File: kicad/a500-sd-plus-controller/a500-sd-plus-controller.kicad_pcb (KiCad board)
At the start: 2 copper layers, 65 x 54 mm, 57 parts, among them J1 Micro_SD_Card_Det2, J2 AUX_SPI, J3 Micro_SD_Card_Det2, J4 JTAG, J5 Conn_01x02, K1 DIP_socket_40pins, U1 RT9013-18, U10 RT9013-33, U2 5M160ZE64, U3 SN74LVC8T245, U4 CSG8520_CIA, U5 SRV05-4, U6 SN74LVC8T245, U7 RT9013-33, U8 RT9013-33, Y1 16MHz

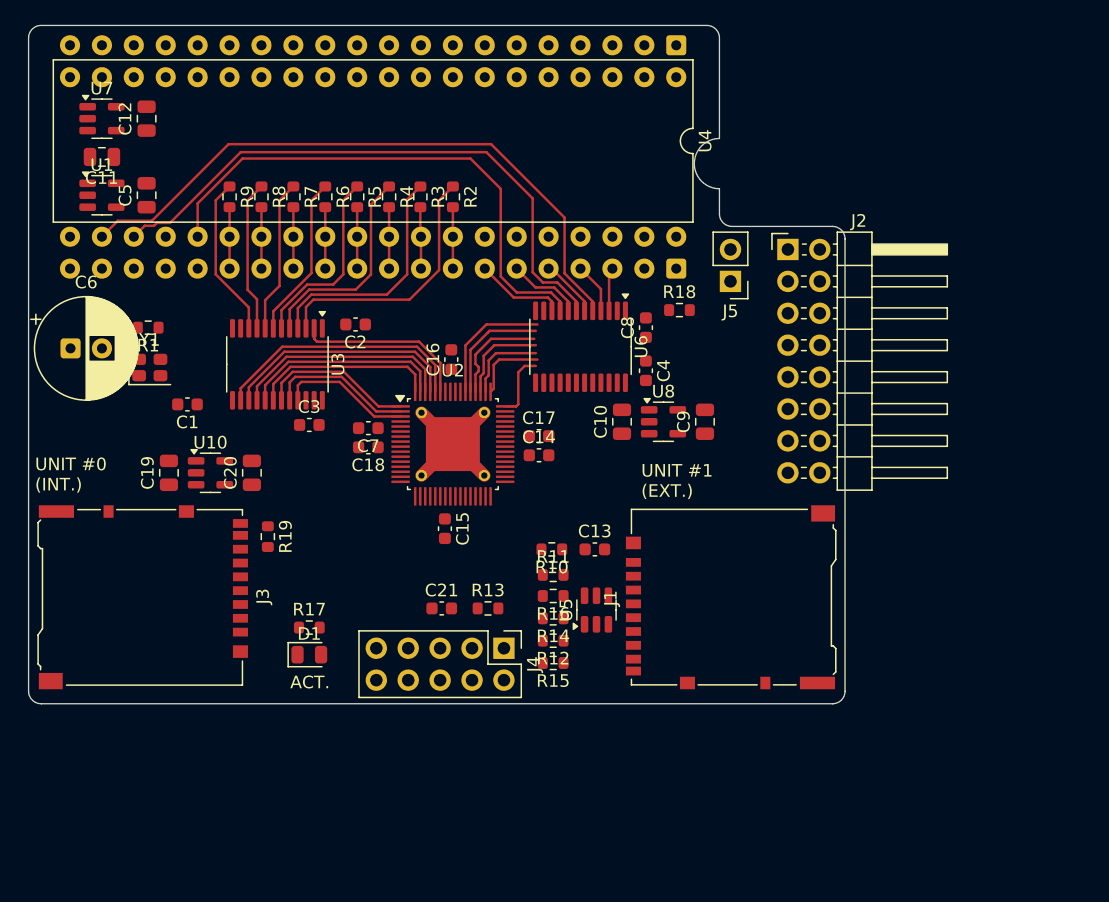
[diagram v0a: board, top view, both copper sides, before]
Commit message: added add ethernet controller
still work in progress
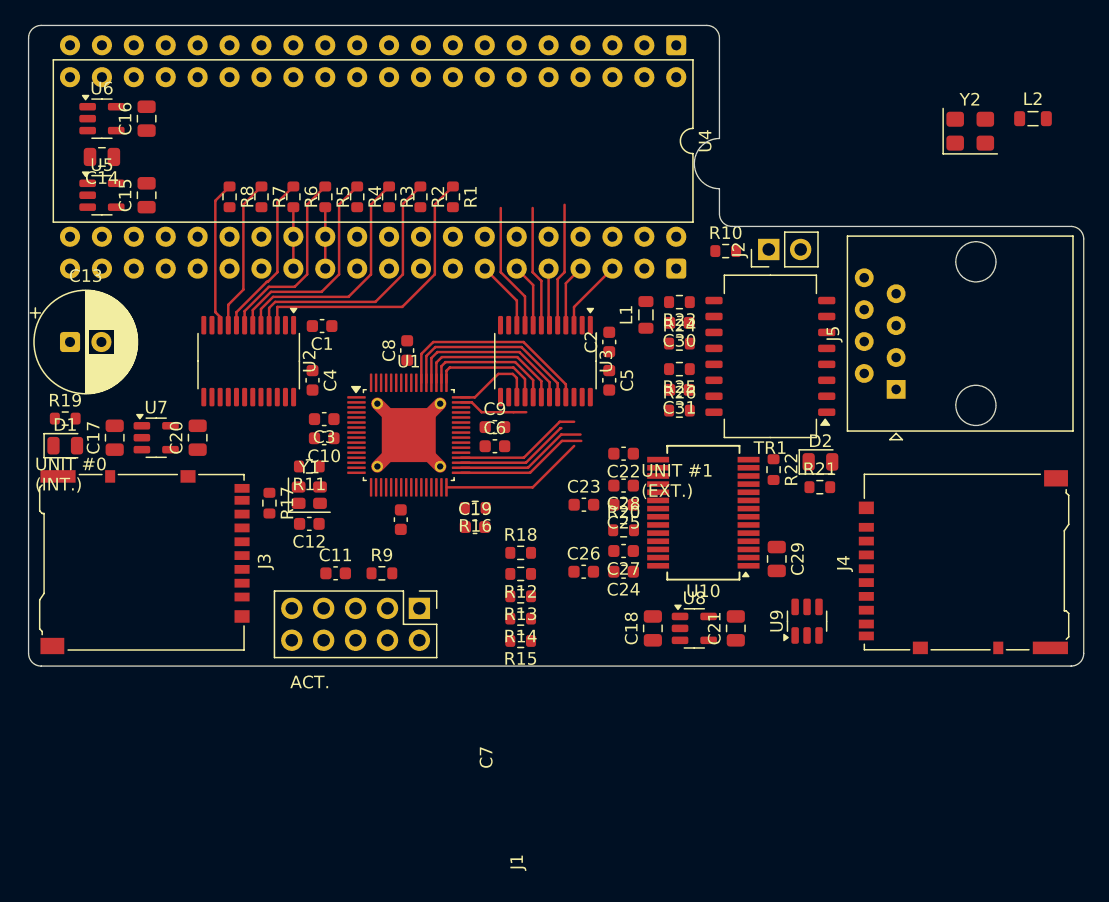
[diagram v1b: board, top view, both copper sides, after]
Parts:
- removed the J2 at (171.4, 84.8)
- added C22: 100nF, Capacitor_SMD:C_0603_1608Metric, F.Cu at (158.4, 101.1)
- added C23: 22p, Capacitor_SMD:C_0603_1608Metric, F.Cu at (155.2, 105.2)
- added C24: 100nF, Capacitor_SMD:C_0603_1608Metric, F.Cu at (158.4, 110.5)
- added C25: 100nF, Capacitor_SMD:C_0603_1608Metric, F.Cu at (158.4, 105.2)
- added C26: 22p, Capacitor_SMD:C_0603_1608Metric, F.Cu at (155.2, 110.5)
- added C27: 100nF, Capacitor_SMD:C_0603_1608Metric, F.Cu at (158.4, 108.8)
- added C28: 100nF, Capacitor_SMD:C_0603_1608Metric, F.Cu at (158.4, 103.6)
- added C29: 10uF, Capacitor_SMD:C_0805_2012Metric, F.Cu at (170.6, 109.5)
- added C30: 100nF, Capacitor_SMD:C_0603_1608Metric, F.Cu at (162.8, 90.7)
- added C31: 100nF, Capacitor_SMD:C_0603_1608Metric, F.Cu at (162.8, 96.0)
- added D2: RED, LED_SMD:LED_0805_2012Metric, F.Cu at (174.0, 101.7)
- added J5: RJ45, Connector_RJ:RJ45_Amphenol_54602-x08_Horizontal, F.Cu at (180.1, 96.0)
- added L1: L_Ferrite, Inductor_SMD:L_0805_2012Metric, F.Cu at (160.1, 90.0)
- added L2: L_Ferrite, Inductor_SMD:L_0805_2012Metric, F.Cu at (191.0, 74.4)
- added R20: 0E, Resistor_SMD:R_0603_1608Metric, F.Cu at (158.4, 107.2)
- added R21: 100E, Resistor_SMD:R_0603_1608Metric, F.Cu at (174.0, 103.8)
- added R22: 2K32, Resistor_SMD:R_0603_1608Metric, F.Cu at (170.3, 102.4)
- added R23: 49K9, Resistor_SMD:R_0603_1608Metric, F.Cu at (162.8, 89.0)
- added R24: 49K9, Resistor_SMD:R_0603_1608Metric, F.Cu at (162.8, 92.3)
- added R25: 49K9, Resistor_SMD:R_0603_1608Metric, F.Cu at (162.8, 94.4)
- added R26: 49K9, Resistor_SMD:R_0603_1608Metric, F.Cu at (162.8, 97.7)
- added TR1: TG110-E050N5xx, Transformer_SMD:Transformer_Ethernet_Halo_N5_SO-16_7.11x12.7mm, F.Cu at (170.1, 93.3)
- added U10: ENC28J60x-SS, Package_SO:SSOP-28_5.3x10.2mm_P0.65mm, F.Cu at (164.7, 105.8)
- added Y2: 25.0MHz, Crystal:Crystal_SMD_SeikoEpson_FA238V-4Pin_3.2x2.5mm, F.Cu at (186.0, 75.4)
- U2: renamed from U3; value SN74LVC8T245 -> SN74LVC4245A
- U3: renamed from U6; value SN74LVC8T245 -> SN74LVC4245A
- moved D1 25.6 mm to (113.9, 100.5)
- moved R19 25.6 mm to (113.9, 98.3)
- moved J4 18.8 mm to (185.4, 109.7)
- moved R11 16.9 mm to (133.3, 102.1)
- moved U9 16.8 mm to (173.0, 114.4)
- moved C18 16.6 mm to (160.7, 115.0)
- moved C21 16.6 mm to (167.3, 115.0)
- moved U8 16.6 mm to (164.0, 115.0)
- moved Y1 16.3 mm to (133.3, 104.4)
- moved C12 13.6 mm to (133.3, 106.7)
- moved C19 9.70 mm to (146.5, 106.9)
- moved R9 8.90 mm to (139.1, 110.6)
- moved C11 8.90 mm to (135.4, 110.6)
- moved C1 7.94 mm to (134.4, 90.9), turned to 180 degrees
- moved J1 7.44 mm to (142.1, 113.4)
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- renumbered C3 to C1, C18 to C10, C21 to C11, C1 to C12, C6 to C13, C11 to C14, C5 to C15, C12 to C16, C19 to C17, C10 to C18, C13 to C19, C8 to C2, C9 to C21, C7 to C3, C2 to C4, C4 to C5, C14 to C6, C15 to C7, C16 to C8, C17 to C9, J4 to J1, J5 to J2, J1 to J4, R2 to R1, R18 to R10, R1 to R11, R16 to R12, R14 to R13, R12 to R14, R10 to R16, R19 to R17, R11 to R18, R17 to R19, R3 to R2, R4 to R3, R5 to R4, R6 to R5, R7 to R6, R8 to R7, R9 to R8, R13 to R9, U2 to U1, U1 to U5, U7 to U6, U10 to U7, U5 to U9
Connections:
- net /CTRL.~{CS} renamed /CTRL.~{CS_MB}
- net Net-(U2A-IO_/_CLK3) renamed /16MHz
- C2 pad 2: +3.3V -> VCC
- C5 pad 2: VCC -> +3.3V
- K1 pad 18: /Mainboard interface/~{CS} -> /Mainboard interface/~{CS_MB}
- U1 pad 11: unconnected-(U2A-IO-Pad11) -> /CTRL.~{CS_CIA}
- U1 pad 24: unconnected-(U2A-IO-Pad24) -> /ETH_1.MISO
- U1 pad 33: /AUX.~{CS2} -> unconnected-(U1A-IO-Pad33)
- U1 pad 34: /AUX.~{CS1} -> unconnected-(U1A-IO-Pad34)
- U1 pad 35: /AUX.SCLK -> unconnected-(U1A-IO-Pad35)
- U1 pad 36: /AUX.MISO -> /Ethernet/ETH.~{RST}
- U1 pad 37: /AUX.MOSI -> unconnected-(U1A-IO-Pad37)
- U3 pad 1: +3.3V -> VCC
- U3 pad 2: GND -> VCC
- U3 pad 23: VCC -> +3.3V
- U3 pad 24: VCC -> +3.3V
- U3 pad 7: /Mainboard interface/~{CS} -> /Mainboard interface/~{CS_MB}
- U4 pad 23: /Mainboard interface/~{CS} -> /CTRL.~{CS_CIA}
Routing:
- net /Mainboard interface/~{CS}: track 47.1 -> 0.00 mm
- net /Mainboard interface/R/~{W}: track 50.7 -> 9.81 mm
- net /Mainboard interface/E: track 42.5 -> 10.1 mm
- net /DD7: track 20.6 -> 0.00 mm
- net /DD6: track 19.1 -> 0.00 mm
- net /DD5: track 17.7 -> 0.00 mm
- net /DD4: track 16.3 -> 0.00 mm
- net /DD3: track 14.8 -> 0.00 mm
- net /CTRL.DIR: track 14.0 -> 0.00 mm
- net /DD2: track 12.4 -> 0.00 mm
- net /DD1: track 11.6 -> 0.00 mm
- net unconnected-(U1A-IO-Pad32): track 0.00 -> 11.5 mm
- net /DD0: track 10.6 -> 0.00 mm
- net unconnected-(U1A-IO-Pad33): track 0.00 -> 10.6 mm
- net unconnected-(U1A-IO-Pad34): track 0.00 -> 10.6 mm
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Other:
- board size 65 x 54 mm -> 84 x 51 mm

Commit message: routing completely done
todo: review footprints and cleanup silkscreen
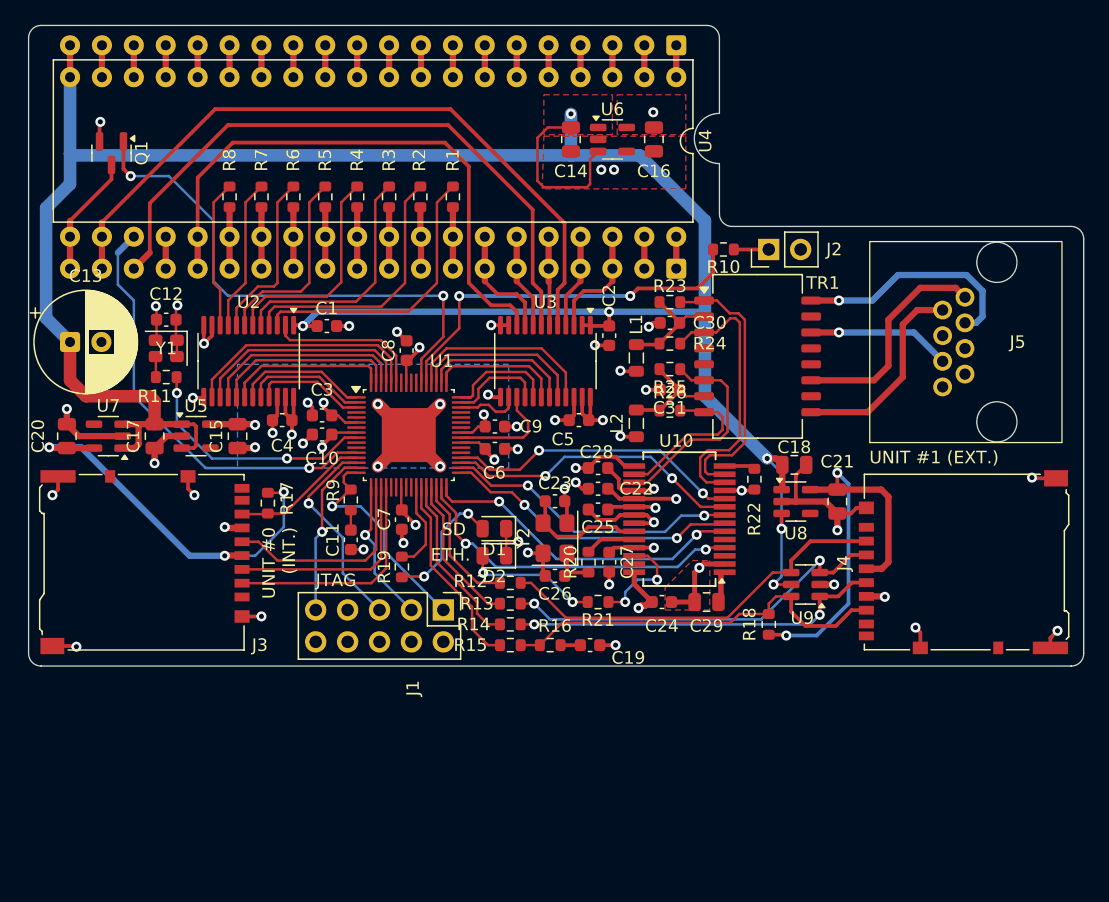
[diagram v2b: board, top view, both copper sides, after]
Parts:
- added Q1: BSS138, Package_TO_SOT_SMD:SOT-23, F.Cu at (117.6, 77.2)
- J5: footprint Connector_RJ:RJ45_Amphenol_54602-x08_Horizontal -> Library:R-RJ45R08P-A004
- L1, L2: value L_Ferrite -> 600R@100MHz
- TR1: value TG110-E050N5xx -> H1102NLT; footprint Transformer_SMD:Transformer_Ethernet_Halo_N5_SO-16_7.11x12.7mm -> Transformer_SMD:Transformer_Ethernet_Bourns_PT61017PEL
- moved Y2 46.3 mm to (152.9, 107.8), turned to 90 degrees
- moved U6 40.7 mm to (157.5, 76.1)
- moved C16 40.4 mm to (160.8, 76.1)
- moved L2 39.8 mm to (159.4, 98.7), turned to 90 degrees
- moved C14 37.4 mm to (154.2, 76.1), turned to 90 degrees
- moved D1 34.8 mm to (148.1, 107.1), turned to 180 degrees
- moved R19 29.3 mm to (140.7, 110.1), turned to -90 degrees
- moved D2 27.0 mm to (148.1, 109.2), turned to 180 degrees
- moved U5 20.6 mm to (124.3, 99.7)
- moved R18 20.6 mm to (169.9, 114.7), turned to 90 degrees
- moved C15 20.5 mm to (127.6, 99.7)
- moved R21 19.9 mm to (156.3, 112.9), turned to 180 degrees
- moved C12 19.8 mm to (122.0, 90.4), turned to 0 degrees
- moved C18 17.2 mm to (172.0, 102.0), turned to 180 degrees
- moved Y1 16.3 mm to (122.0, 92.7), turned to 180 degrees
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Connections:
- C30 pad 1: Net-(TR1-C_RD) -> Net-(TR1-C_TD)
- C31 pad 1: Net-(TR1-C_TD) -> Net-(TR1-C_RD)
- J5 pad 1: unconnected-(J5-Pad1) -> /Ethernet/TX+
- J5 pad 2: unconnected-(J5-Pad2) -> /Ethernet/TX-
- J5 pad 3: unconnected-(J5-Pad3) -> /Ethernet/RX+
- J5 pad 6: unconnected-(J5-Pad6) -> /Ethernet/RX-
- L1 pad 2: Net-(TR1-C_RD) -> Net-(TR1-C_TD)
- L2 pad 2: Net-(TR1-C_TD) -> Net-(TR1-C_RD)
- R10 pad 1: unconnected-(R10-Pad1) -> /DRIVE_LED
- R23 pad 1: Net-(TR1-RD+) -> Net-(TR1-TD+)
- R23 pad 2: Net-(TR1-C_RD) -> Net-(TR1-C_TD)
- R24 pad 1: Net-(TR1-C_RD) -> Net-(TR1-C_TD)
- R24 pad 2: Net-(TR1-RD-) -> Net-(TR1-TD-)
- R25 pad 1: Net-(TR1-TD+) -> Net-(TR1-RD+)
- R25 pad 2: Net-(TR1-C_TD) -> Net-(TR1-C_RD)
- R26 pad 1: Net-(TR1-C_TD) -> Net-(TR1-C_RD)
- R26 pad 2: Net-(TR1-TD-) -> Net-(TR1-RD-)
- TR1 pad 1: unconnected-(TR1-TX--Pad1) -> Net-(TR1-TD+)
- TR1 pad 10: Net-(TR1-C_RD) -> unconnected-(TR1-C_RX-Pad10)
- TR1 pad 11: Net-(TR1-RD-) -> /Ethernet/TX+
- TR1 pad 12: unconnected-(TR1-NC-Pad12) -> (no net)
- TR1 pad 13: unconnected-(TR1-NC-Pad13) -> (no net)
- TR1 pad 14: Net-(TR1-TD+) -> /Ethernet/RX-
- TR1 pad 15: Net-(TR1-C_TD) -> unconnected-(TR1-C_TX-Pad15)
- TR1 pad 16: Net-(TR1-TD-) -> /Ethernet/RX+
- TR1 pad 2: unconnected-(TR1-C_TX-Pad2) -> Net-(TR1-C_TD)
- TR1 pad 3: unconnected-(TR1-TX+-Pad3) -> Net-(TR1-TD-)
- TR1 pad 4: unconnected-(TR1-NC-Pad4) -> (no net)
- TR1 pad 5: unconnected-(TR1-NC-Pad5) -> (no net)
- TR1 pad 6: unconnected-(TR1-RX--Pad6) -> Net-(TR1-RD+)
- TR1 pad 7: unconnected-(TR1-C_RX-Pad7) -> Net-(TR1-C_RD)
- TR1 pad 8: unconnected-(TR1-RX+-Pad8) -> Net-(TR1-RD-)
- TR1 pad 9: Net-(TR1-RD+) -> /Ethernet/TX-
- U1 pad 11: /CTRL.~{CS_CIA} -> unconnected-(U1A-IO-Pad11)
- U1 pad 12: /SD.MISO1 -> /CTRL.~{CS_CIA}
- U1 pad 13: /SD.SCLK1 -> /SD.MISO1
- U1 pad 18: /SD.MOSI1 -> /SD.SCLK1
- U1 pad 19: /SD.~{CS1} -> /SD.MOSI1
- U1 pad 20: unconnected-(U1A-IO-Pad20) -> /SD.~{CS1}
- U1 pad 24: /ETH_1.MISO -> unconnected-(U1A-IO-Pad24)
- U1 pad 26: unconnected-(U1A-IO-Pad26) -> /SD.LED
- U1 pad 31: /SD.LED -> /Ethernet/ETH.~{INT}
- U1 pad 32: unconnected-(U1A-IO-Pad32) -> /Ethernet/ETH.MISO
- U1 pad 33: unconnected-(U1A-IO-Pad33) -> /Ethernet/ETH.MOSI
- U1 pad 34: unconnected-(U1A-IO-Pad34) -> /Ethernet/ETH.SCLK
- U1 pad 35: unconnected-(U1A-IO-Pad35) -> /Ethernet/ETH.~{CS}
- U1 pad 42: /16MHz -> unconnected-(U1A-IO_/_CLK3-Pad42)
- U1 pad 46: unconnected-(U1A-IO-Pad46) -> /CTRL.E
- U1 pad 47: unconnected-(U1A-IO-Pad47) -> /CTRL.RS3
- U1 pad 48: /CTRL.E -> /CTRL.~{CS_MB}
- U1 pad 49: /CTRL.RS3 -> /CTRL.RS2
- U1 pad 50: /CTRL.~{CS_MB} -> /CTRL.R/~{W}
- U1 pad 51: /CTRL.RS2 -> /CTRL.RS1
- U1 pad 52: /CTRL.R/~{W} -> /CTRL.RS0
- U1 pad 53: /CTRL.RS1 -> /DRIVE_LED
- U1 pad 54: /CTRL.RS0 -> /CTRL.INT
- U1 pad 9: unconnected-(U1A-IO_/_CLK1-Pad9) -> /16MHz
- U10 pad 12: Net-(TR1-RD-) -> Net-(TR1-TD-)
- U10 pad 13: Net-(TR1-RD+) -> Net-(TR1-TD+)
- U10 pad 16: Net-(TR1-TD-) -> Net-(TR1-RD-)
- U10 pad 17: Net-(TR1-TD+) -> Net-(TR1-RD+)
- U10 pad 6: /Ethernet/ETH.MOSI -> /Ethernet/ETH.MISO
- U3 pad 10: /Mainboard interface/~{RESET} -> /Mainboard interface/E
- U3 pad 14: /CTRL.~{RESET} -> /CTRL.E
- U3 pad 15: /CTRL.E -> /CTRL.~{RESET}
- U3 pad 9: /Mainboard interface/E -> /Mainboard interface/~{RESET}
- U9 pad 3: Net-(J4-DAT3/CD) -> Net-(J4-CMD)
- U9 pad 4: Net-(J4-CMD) -> Net-(J4-DAT3/CD)
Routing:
- net VCC: track 0.00 -> 194.3 mm, vias 0 -> 6
- net GND: track 0.00 -> 117.5 mm, vias 0 -> 48
- net +3.3V: track 0.00 -> 53.2 mm, vias 0 -> 15
- net /Mainboard interface/R/~{W}: track 9.81 -> 56.4 mm
- net /CTRL.INT: track 0.00 -> 42.3 mm, vias 0 -> 2
- net /Mainboard interface/~{CS_MB}: track 9.62 -> 51.1 mm
- net /Mainboard interface/E: track 10.1 -> 45.9 mm
- net /CTRL.~{CS_CIA}: track 0.00 -> 34.4 mm, vias 0 -> 1
- net /micro-sd/+3V3_SD2: track 0.00 -> 33.2 mm, vias 0 -> 2
- net /micro-sd/+3V3_SD1: track 0.00 -> 32.3 mm, vias 0 -> 3
- net Net-(J4-DAT0): track 0.00 -> 31.8 mm
- net Net-(J4-DAT3/CD): track 0.00 -> 31.8 mm
- net Net-(J4-CMD): track 0.00 -> 31.5 mm, vias 0 -> 2
- net /DRIVE_LED: track 0.00 -> 30.8 mm, vias 0 -> 2
- net Net-(J4-CLK): track 0.00 -> 29.8 mm, vias 0 -> 2
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- added copper zone on B.Cu, net +1V8
- added copper zone on F.Cu, net +3.3V
- added copper zone on In2.Cu, net +3.3V
- added copper zone on F.Cu, net GND
- added copper zone on In1.Cu, net GND
- added copper zone on F.Cu, net VCC
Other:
- outline, holes or cut-outs redrawn
- copper layers 2 -> 4
- board text added: "ETH."
- board text added: "JTAG"
- board text added: "SD"
- board text removed: "ACT."

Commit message: cleaned up silkscreen and 3D models
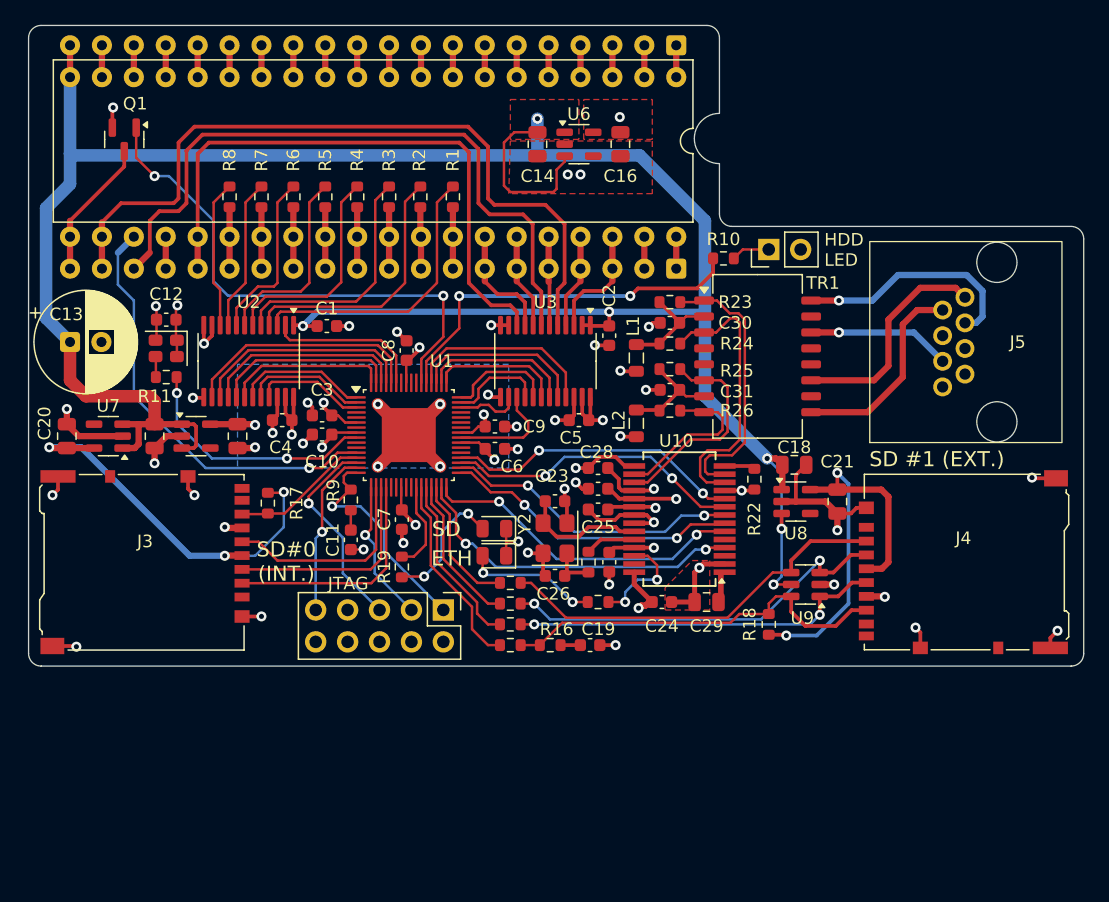
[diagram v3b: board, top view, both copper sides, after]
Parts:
- added REF**: KiCad-Logo_6mm_SilkScreen, Symbol:KiCad-Logo_6mm_SilkScreen, B.Cu at (121.0, 112.4)
- added REF**: OSHW-Symbol_6.7x6mm_SilkScreen, Symbol:OSHW-Symbol_6.7x6mm_SilkScreen, B.Cu at (172.3, 92.6)
- Q1: value BSS138 -> AO3400A
- moved C14 2.69 mm to (151.5, 76.5)
- moved C16 2.69 mm to (158.1, 76.5)
- moved U6 2.69 mm to (154.8, 76.5)
- moved Q1 1.49 mm to (118.6, 76.1)
- moved R10 0.71 mm to (166.3, 85.5)
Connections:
- net /micro-sd/+3V3_SD1 renamed /Micro-SD/+3V3_SD1
- net /micro-sd/+3V3_SD2 renamed /Micro-SD/+3V3_SD2
- Q1 pad 2: unconnected-(Q1-S-Pad2) -> GND
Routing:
- net /Mainboard interface/R/~{W}: track 56.4 -> 60.2 mm
- net /Mainboard interface/~{CS_MB}: track 51.1 -> 53.9 mm
- net /Mainboard interface/E: track 45.9 -> 47.7 mm
- net GND: track 117.5 -> 119.1 mm, vias 48 -> 49
- net unconnected-(Q1-S-Pad2): track 1.58 -> 0.00 mm, vias 1 -> 0
- net /Mainboard interface/~{INT}: track 9.62 -> 11.1 mm
- net /DRIVE_LED: track 30.8 -> 30.1 mm
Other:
- board text added: "A500-SD-PLUS"
- board text added: "CERN-OHL-S V2.0"
- board text added: "ETH"
- board text added: "HDD LED"
- board text added: "MOUNT ON ODD CIA"
- board text added: "Rev 1.0 DvW 2025"
- board text added: "SD #1 (EXT.)"
- board text added: "SD#0 (INT.)"
- board text removed: "ETH."
- board text removed: "UNIT #0 (INT.)"
- board text removed: "UNIT #1 (EXT.)"
